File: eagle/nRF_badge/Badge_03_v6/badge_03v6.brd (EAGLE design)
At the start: 30 x 70 mm, 45 parts, among them U1 LIS2DH12, U2 LP2985LV, U3 MCP6231, U5 M95M02, Y1 32768Hz

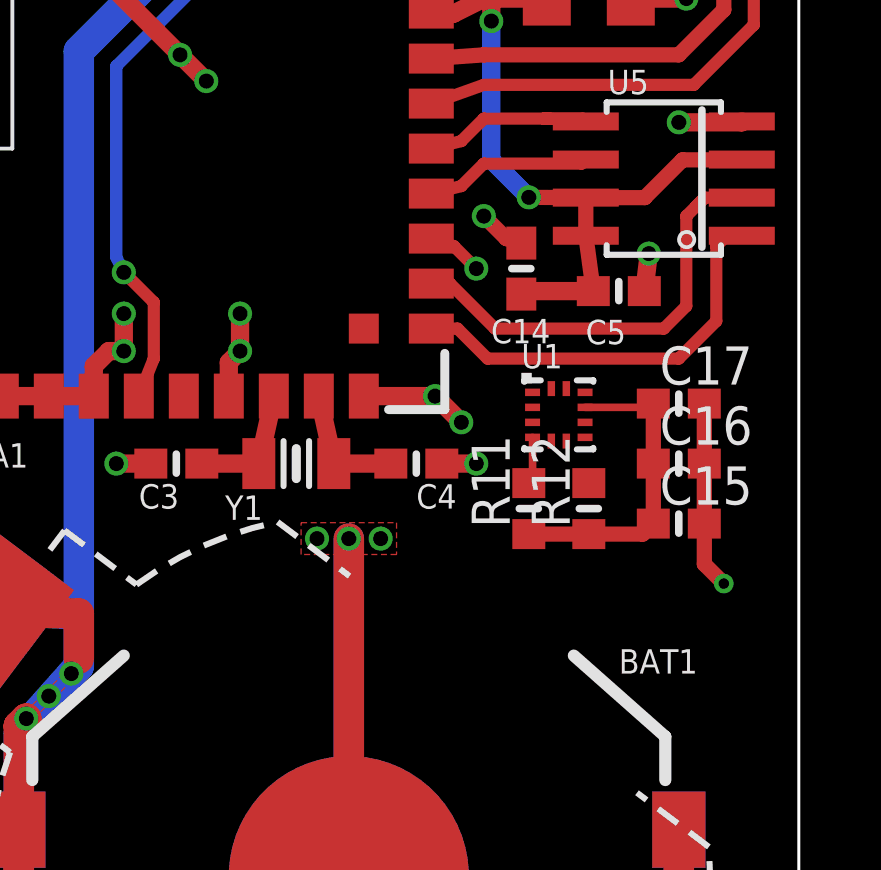
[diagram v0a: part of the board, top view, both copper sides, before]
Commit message: Adding an accelerometer
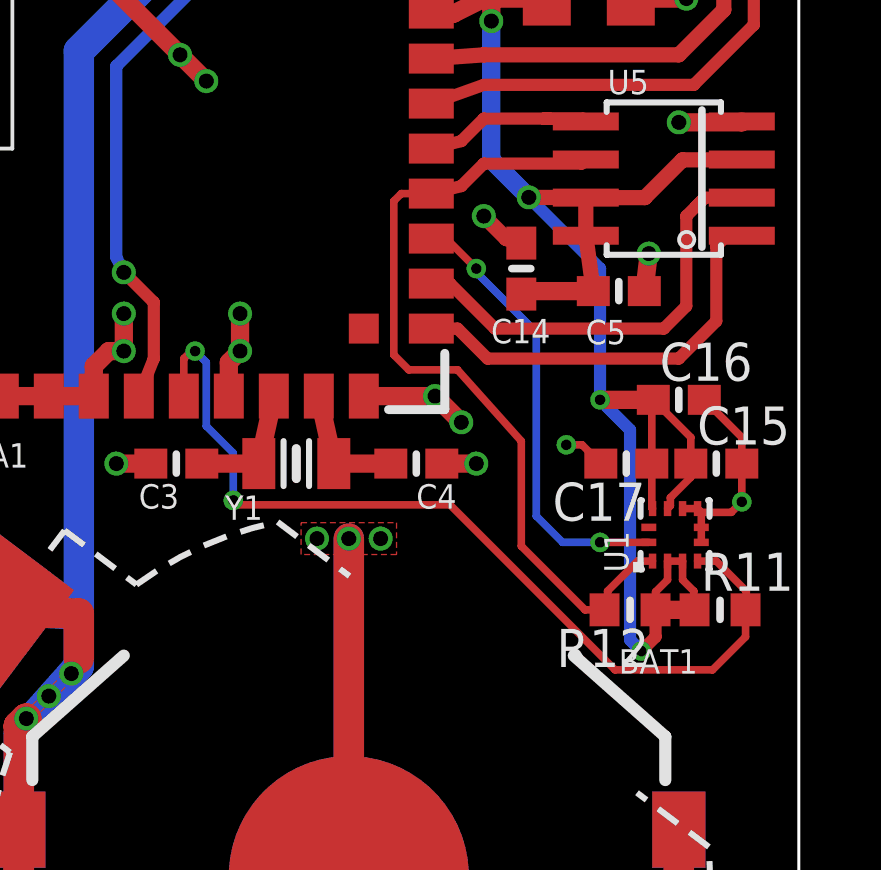
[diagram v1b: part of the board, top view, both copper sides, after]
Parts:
- C15, C17: value 100nF -> 0.1uF
- moved R11 7.21 mm to (27.4, 21.1), turned to 0 degrees
- moved U1 5.57 mm to (25.9, 23.6), turned to 90 degrees
- moved R12 3.64 mm to (24.4, 21.1), turned to 180 degrees
- moved C17 2.66 mm to (24.2, 26.0), turned to 180 degrees
- moved C15 2.36 mm to (27.2, 26.0)
- moved C16 2.12 mm to (26.0, 28.1)
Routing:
- net SDA: track 1.58 -> 30.9 mm, vias 0 -> 2
- net VCC: track 78.5 -> 101.4 mm, vias 2 -> 4
- net SCK: track 5.55 -> 27.4 mm
- net LIS_INT1: track 1.85 -> 15.1 mm, vias 1 -> 2
- net GND: track 93.0 -> 95.2 mm, vias 33 -> 34

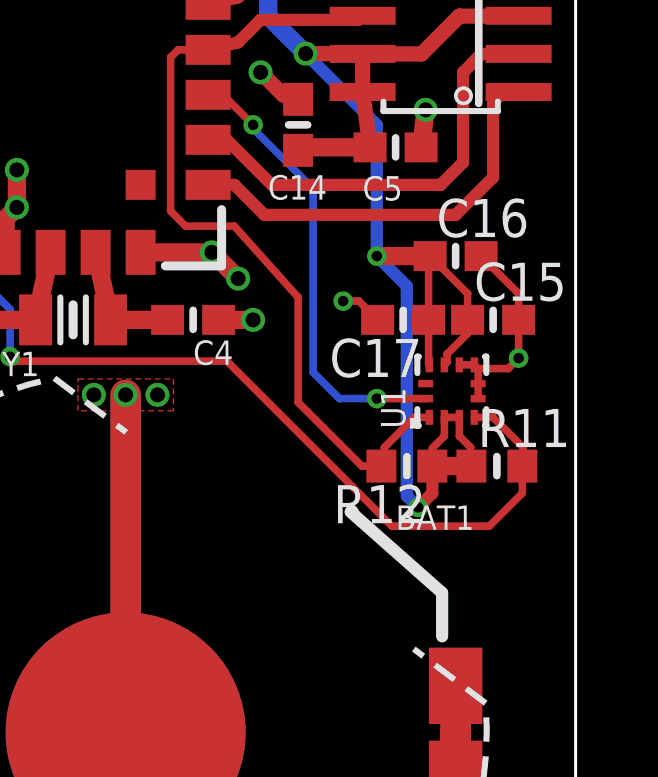
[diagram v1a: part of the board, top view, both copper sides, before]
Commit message: Cleanning up labels
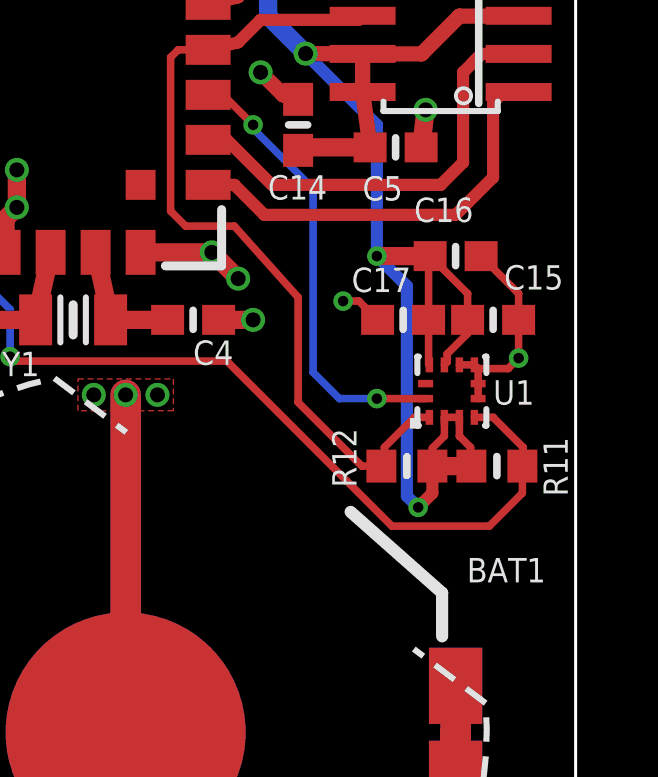
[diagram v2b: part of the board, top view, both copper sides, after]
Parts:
- C15, C17: value 0.1uF -> 0u1
- C16: value 10uF -> 10u
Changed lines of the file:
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@@
 </element>
 <element name="BAT1" library="Badge" package="BATTCON_20MM_4LEGS_ISO_NOCREAM" value="CR2032" x="15" y="12.25" smashed="yes">
-<attribute name="NAME" x="24" y="19" size="0.8128" layer="25" font="vector" ratio="16"/>
+<attribute name="NAME" x="26.375" y="17.25" size="0.8128" layer="25" font="vector" ratio="16"/>
 </element>
 <element name="C1" library="rcl" package="C1206" value="100u" x="23" y="41.5" smashed="yes">
@@
 <attribute name="SF_SKU" value="COM-00597" x="15" y="53" size="1.778" layer="27" rot="R270" display="off"/>
 </element>
-<element name="C15" library="rcl" package="C0603" value="0.1uF" x="27.25" y="26"/>
-<element name="C16" library="rcl" package="C0603" value="10uF" x="26" y="28.125"/>
-<element name="C17" library="rcl" package="C0603" value="0.1uF" x="24.25" y="26" smashed="yes" rot="R180">
-<attribute name="NAME" x="24.885" y="25.365" size="1.27" layer="25" rot="R180"/>
-<attribute name="VALUE" x="22.635" y="26.405" size="1.27" layer="27" rot="R180"/>
+<element name="C15" library="rcl" package="C0603" value="0u1" x="27.25" y="26" smashed="yes">
+<attribute name="NAME" x="27.615" y="27.01" size="0.8128" layer="25" font="vector" ratio="16"/>
+<attribute name="VALUE" x="29.655" y="24.115" size="0.8128" layer="27" font="vector" ratio="16" rot="R90"/>
 </element>
-<element name="R11" library="rcl" package="R0603" value="1k" x="27.375" y="21.125"/>
-<element name="R12" library="rcl" package="R0603" value="1k" x="24.375" y="21.125" rot="R180"/>
-<element name="U1" library="Badge" package="LGA12" value="LIS2DH12" x="25.875" y="23.625" rot="R90"/>
+<element name="C16" library="rcl" package="C0603" value="10u" x="26" y="28.125" smashed="yes">
+<attribute name="NAME" x="24.615" y="29.26" size="0.8128" layer="25" font="vector" ratio="16"/>
+<attribute name="VALUE" x="27.365" y="29.22" size="0.8128" layer="27" font="vector" ratio="16"/>
+</element>
+<element name="C17" library="rcl" package="C0603" value="0u1" x="24.25" y="26" smashed="yes" rot="R180">
+<attribute name="NAME" x="24.51" y="27.74" size="0.8128" layer="25" font="vector" ratio="16" rot="R180"/>
+<attribute name="VALUE" x="21.845" y="26.385" size="0.8128" layer="27" font="vector" ratio="16" rot="R270"/>
+</element>
+<element name="R11" library="rcl" package="R0603" value="1k" x="27.375" y="21.125" smashed="yes">
+<attribute name="NAME" x="29.74" y="20.115" size="0.8128" layer="25" font="vector" ratio="16" rot="R90"/>
+<attribute name="VALUE" x="27.74" y="19.095" size="0.8128" layer="27" font="vector" ratio="16"/>
+</element>
+<element name="R12" library="rcl" package="R0603" value="1k" x="24.375" y="21.125" smashed="yes" rot="R180">
+<attribute name="NAME" x="21.885" y="22.385" size="0.8128" layer="25" font="vector" ratio="16" rot="R270"/>
+<attribute name="VALUE" x="24.26" y="19.905" size="0.8128" layer="27" font="vector" ratio="16" rot="R180"/>
+</element>
+<element name="U1" library="Badge" package="LGA12" value="LIS2DH12" x="25.875" y="23.625" smashed="yes" rot="R90">
+<attribute name="NAME" x="27.25" y="23.175" size="0.8128" layer="25" font="vector" ratio="16"/>
+</element>
 </elements>
 <signals>

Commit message: Exporting gerber and pnp
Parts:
- moved R11 0.12 mm to (27.5, 21.1)
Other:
- board text added: "BAT4"
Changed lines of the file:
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@@
 <rectangle x1="5.25" y1="50.125" x2="6.25" y2="51.5" layer="42"/>
 <text x="9.011" y="33.751" size="1.9304" layer="22" font="vector" ratio="16" rot="MR90" align="top-left">03v6</text>
+<text x="26.125" y="16.125" size="0.8128" layer="25" font="vector" ratio="16">BAT4</text>
 </plain>
 <attributes>
@@
 <attribute name="VALUE" x="8.875" y="58" size="0.8128" layer="27" font="vector" ratio="16"/>
 </element>
-<element name="BAT1" library="Badge" package="BATTCON_20MM_4LEGS_ISO_NOCREAM" value="CR2032" x="15" y="12.25" smashed="yes">
-<attribute name="NAME" x="26.375" y="17.25" size="0.8128" layer="25" font="vector" ratio="16"/>
-</element>
+<element name="BAT1" library="Badge" package="BATTCON_20MM_4LEGS_ISO_NOCREAM" value="CR2032" x="15" y="12.25" smashed="yes"/>
 <element name="C1" library="rcl" package="C1206" value="100u" x="23" y="41.5" smashed="yes">
 <attribute name="NAME" x="19.25" y="41.5" size="0.8128" layer="25" font="vector" ratio="16"/>
@@
 <attribute name="VALUE" x="25.28" y="42.615" size="0.8128" layer="27" font="vector" ratio="16" rot="R90"/>
 </element>
-<element name="BAT4" library="Badge" package="BU2032SM_CREAM" value="CR2032" x="15" y="12.25" rot="R323"/>
+<element name="BAT4" library="Badge" package="BU2032SM_CREAM" value="CR2032" x="15" y="12.25" smashed="yes" rot="R323"/>
 <element name="MIC_F" library="Badge" package="TESTPOINT" value="" x="23.375" y="59"/>
 <element name="M_VCC" library="Badge" package="TESTPOINT" value="" x="26.125" y="44.625"/>
@@
 <attribute name="VALUE" x="21.845" y="26.385" size="0.8128" layer="27" font="vector" ratio="16" rot="R270"/>
 </element>
-<element name="R11" library="rcl" package="R0603" value="1k" x="27.375" y="21.125" smashed="yes">
-<attribute name="NAME" x="29.74" y="20.115" size="0.8128" layer="25" font="vector" ratio="16" rot="R90"/>
-<attribute name="VALUE" x="27.74" y="19.095" size="0.8128" layer="27" font="vector" ratio="16"/>
+<element name="R11" library="rcl" package="R0603" value="1k" x="27.5" y="21.125" smashed="yes">
+<attribute name="NAME" x="25.865" y="19.135" size="0.8128" layer="25" font="vector" ratio="16"/>
+<attribute name="VALUE" x="28.365" y="19.135" size="0.8128" layer="27" font="vector" ratio="16"/>
 </element>
 <element name="R12" library="rcl" package="R0603" value="1k" x="24.375" y="21.125" smashed="yes" rot="R180">
@@
 <wire x1="26.125" y1="22.125" x2="26.5" y2="21.75" width="0.254" layer="1"/>
 <wire x1="26.5" y1="21.75" x2="26.5" y2="21.15" width="0.254" layer="1"/>
-<wire x1="26.525" y1="21.125" x2="26.5" y2="21.15" width="0.254" layer="1"/>
+<wire x1="26.65" y1="21.125" x2="26.5" y2="21.15" width="0.254" layer="1"/>
 <wire x1="25.1" y1="24.525" x2="25.1" y2="26" width="0.254" layer="1"/>
 <wire x1="25.125" y1="24.5" x2="25.1" y2="24.525" width="0.254" layer="1"/>
@@
 <wire x1="25.15" y1="28.125" x2="23.375" y2="28.125" width="0.6096" layer="1"/>
 <via x="24.75" y="19.75" extent="1-16" drill="0.35"/>
-<wire x1="25.225" y1="21.125" x2="26.525" y2="21.125" width="0.6096" layer="1"/>
+<wire x1="25.225" y1="21.125" x2="26.65" y2="21.125" width="0.6096" layer="1"/>
 <wire x1="21" y1="34.875" x2="23.375" y2="32.5" width="0.4064" layer="16"/>
 <wire x1="23.375" y1="32.5" x2="23.375" y2="28.125" width="0.4064" layer="16"/>
@@
 <wire x1="27.25" y1="22.75" x2="28.25" y2="21.75" width="0.254" layer="1"/>
 <wire x1="28.25" y1="21.75" x2="28.25" y2="21.15" width="0.254" layer="1"/>
-<wire x1="28.25" y1="21.15" x2="28.225" y2="21.125" width="0.254" layer="1"/>
-<wire x1="28.225" y1="21.125" x2="27.97013125" y2="21.125" width="0.254" layer="1"/>
-<wire x1="28.225" y1="20.225" x2="28.225" y2="21.125" width="0.254" layer="1"/>
+<wire x1="28.25" y1="21.15" x2="28.35" y2="21.125" width="0.254" layer="1"/>
+<wire x1="28.35" y1="21.125" x2="27.97013125" y2="21.125" width="0.254" layer="1"/>
+<wire x1="28.35" y1="20.225" x2="28.35" y2="21.125" width="0.254" layer="1"/>
 <wire x1="11.14823125" y1="24.77323125" x2="11.2964625" y2="24.625" width="0.254" layer="1"/>
 <wire x1="11.2964625" y1="24.625" x2="18.375" y2="24.625" width="0.254" layer="1"/>
-<wire x1="23.875" y1="19.125" x2="27.125" y2="19.125" width="0.254" layer="1"/>
+<wire x1="23.875" y1="19.125" x2="27.25" y2="19.125" width="0.254" layer="1"/>
 <wire x1="18.375" y1="24.625" x2="23.875" y2="19.125" width="0.254" layer="1"/>
-<wire x1="27.125" y1="19.125" x2="28.225" y2="20.225" width="0.254" layer="1"/>
+<wire x1="27.25" y1="19.125" x2="28.35" y2="20.225" width="0.254" layer="1"/>
 </signal>
 <signal name="CS">

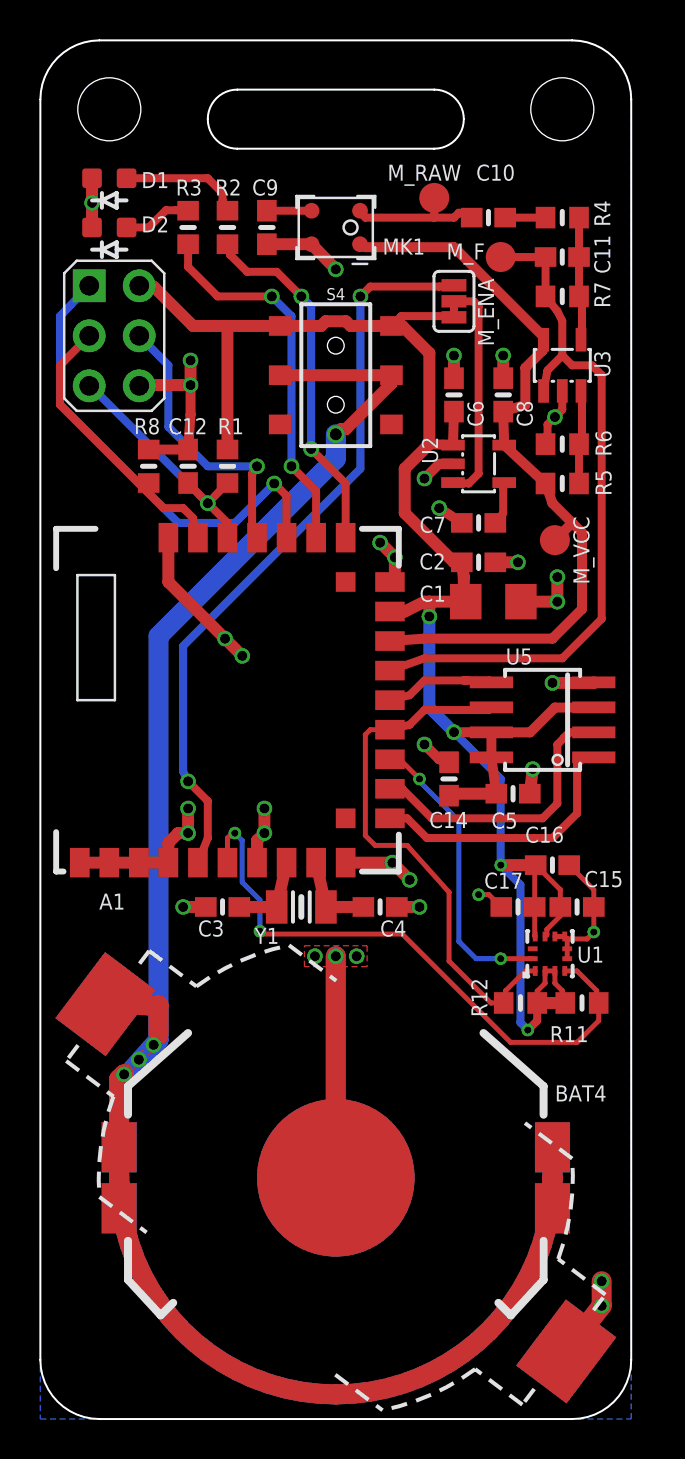
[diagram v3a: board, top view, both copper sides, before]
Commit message: Re-routed LIS2DH12 to use SPI
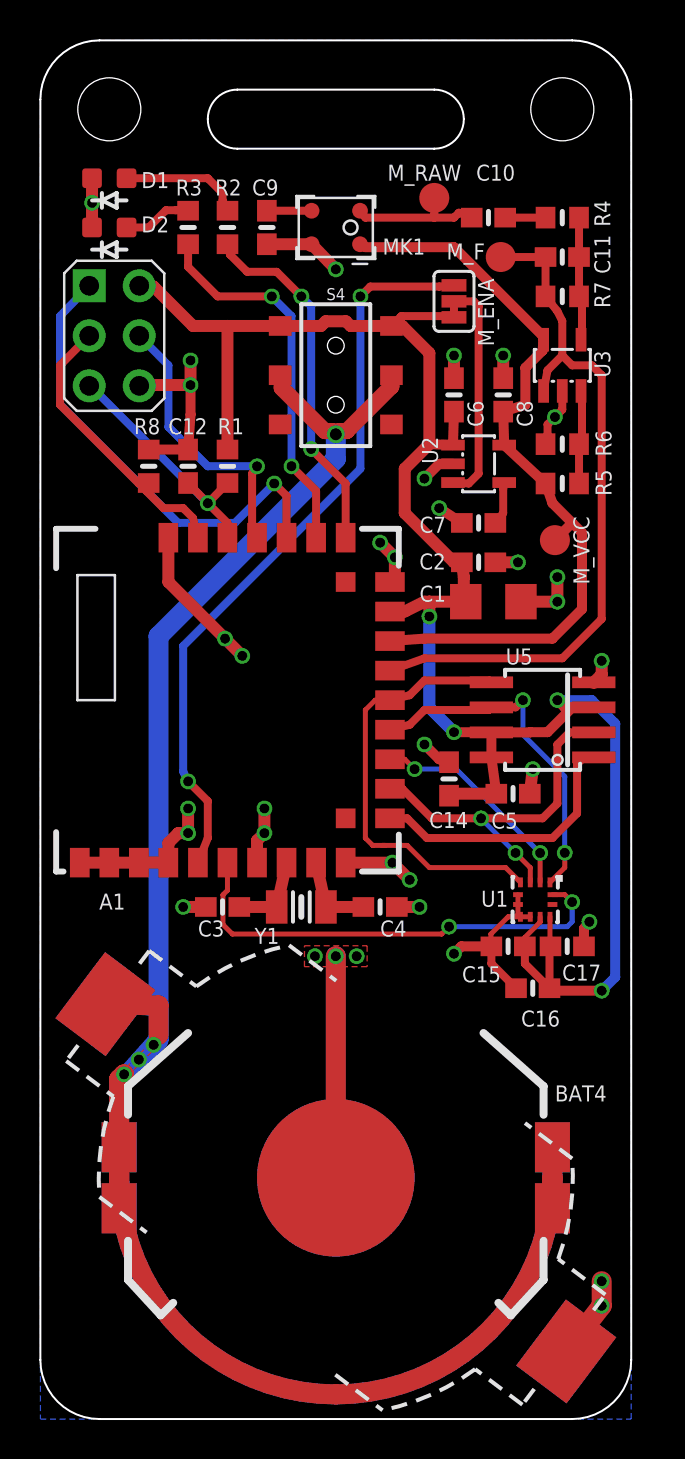
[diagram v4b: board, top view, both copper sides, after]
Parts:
- removed R11, R12: 1k, rcl:R0603
- moved C16 6.33 mm to (25.0, 21.9), turned to 180 degrees
- moved C15 4.03 mm to (23.8, 24.0), turned to 180 degrees
- moved C17 3.20 mm to (26.8, 24.0), turned to 0 degrees
- moved U1 2.85 mm to (25.1, 26.4), turned to 270 degrees
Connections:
- removed net SDA: A1.P$6, R11.2, U1.4
- new net CS1: A1.P$13, U1.2
- net LIS_INT1: now also A1.P$6; no longer A1.P$13
- net MISO: now also U1.3
- net MOSI: now also U1.4
- net SCK: no longer R12.2
- net VCC: no longer R11.1, R12.1, U1.2, U1.3
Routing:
- net SDA: track 31.3 -> 0.00 mm, vias 2 -> 0
- net MOSI: track 5.78 -> 22.4 mm
- net CS1: track 0.00 -> 11.1 mm, vias 0 -> 2
- net SCK: track 27.4 -> 17.7 mm, vias 0 -> 2
- net LIS_INT1: track 15.1 -> 23.6 mm
- net MISO: track 14.8 -> 18.8 mm, vias 0 -> 2
- net VCC: track 101.6 -> 98.0 mm
- net GND: track 95.2 -> 96.1 mm
- net VBATT: track 140.9 -> 140.2 mm

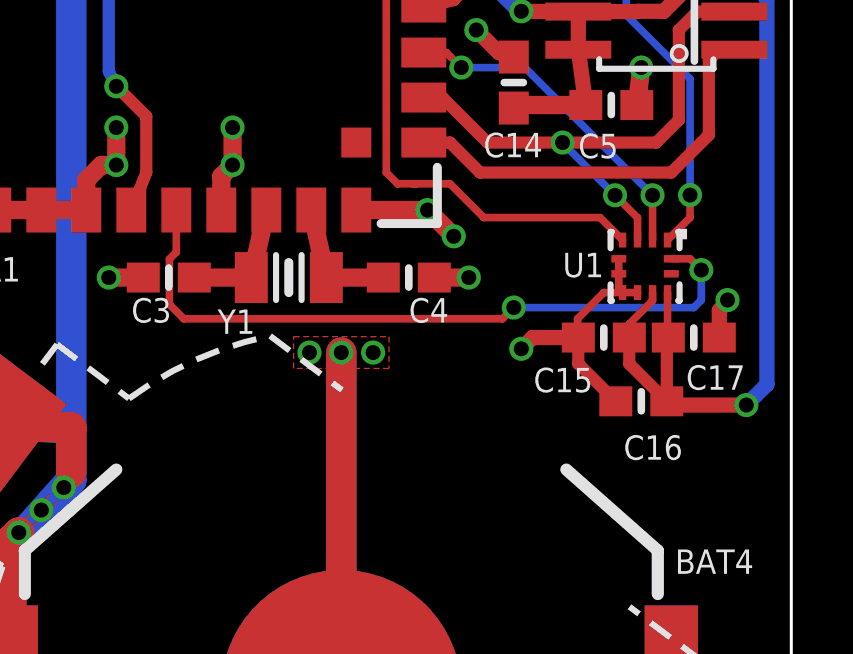
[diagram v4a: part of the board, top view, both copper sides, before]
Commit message: Traces cleanup
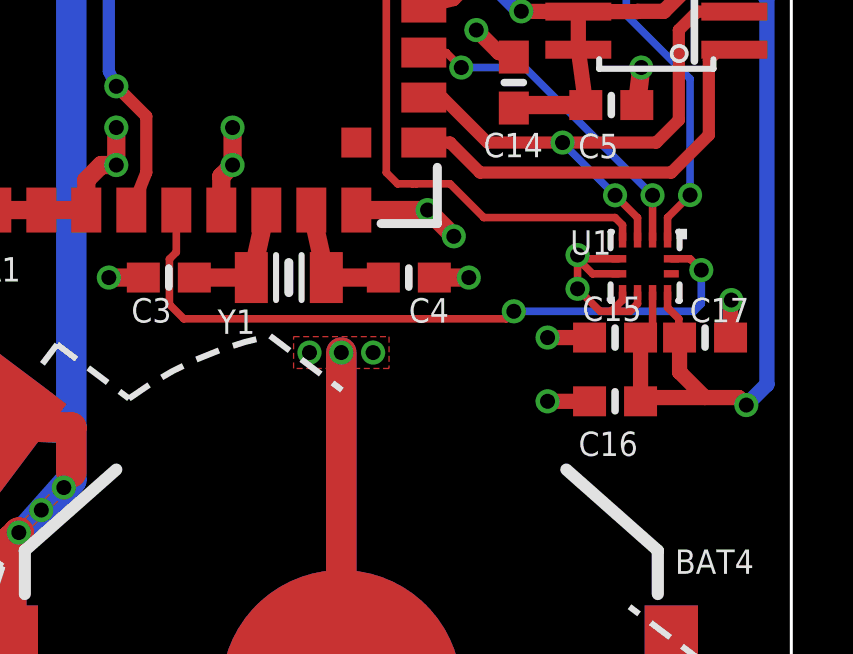
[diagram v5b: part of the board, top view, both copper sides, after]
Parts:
- moved C16 0.88 mm to (24.1, 21.9)
- moved C15 0.38 mm to (24.1, 24.0)
- moved C17 0.38 mm to (27.1, 24.0)
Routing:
- net GND: track 96.1 -> 97.6 mm, vias 34 -> 37
- net VCC: track 98.0 -> 98.5 mm
